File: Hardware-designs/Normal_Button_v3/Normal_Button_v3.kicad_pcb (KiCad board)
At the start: 2 copper layers, 74.2 x 74.2 mm, 40 parts, among them J1 UART, J2 Bat, J3 USB_C, Q1 MMBT3904, SW1 main, SW2 Aux, SW3 Side 1, SW4 Side 2, U1 ESP32-WROOM-32, U2 TP4057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

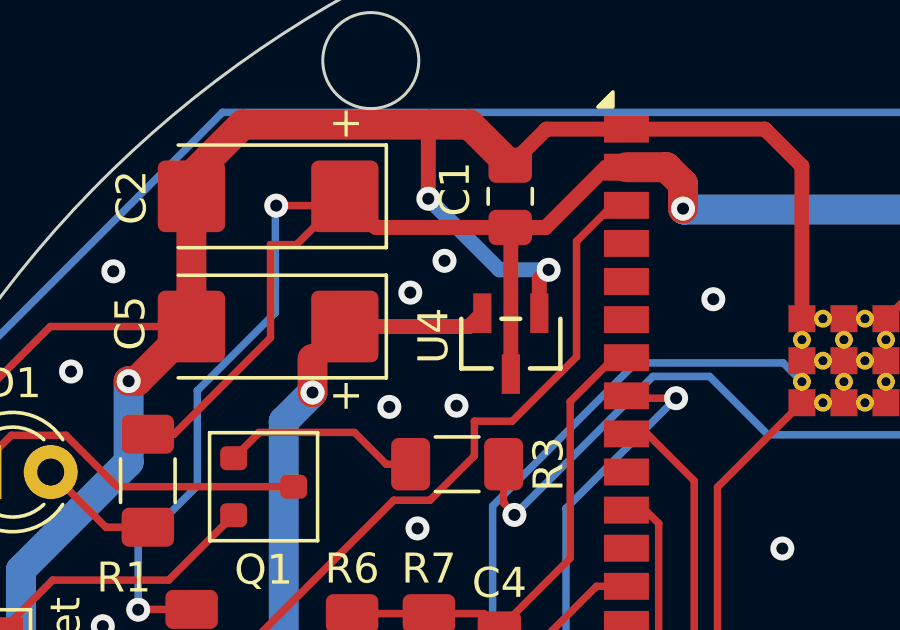
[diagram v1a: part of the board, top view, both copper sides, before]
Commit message: correction voltage regulator
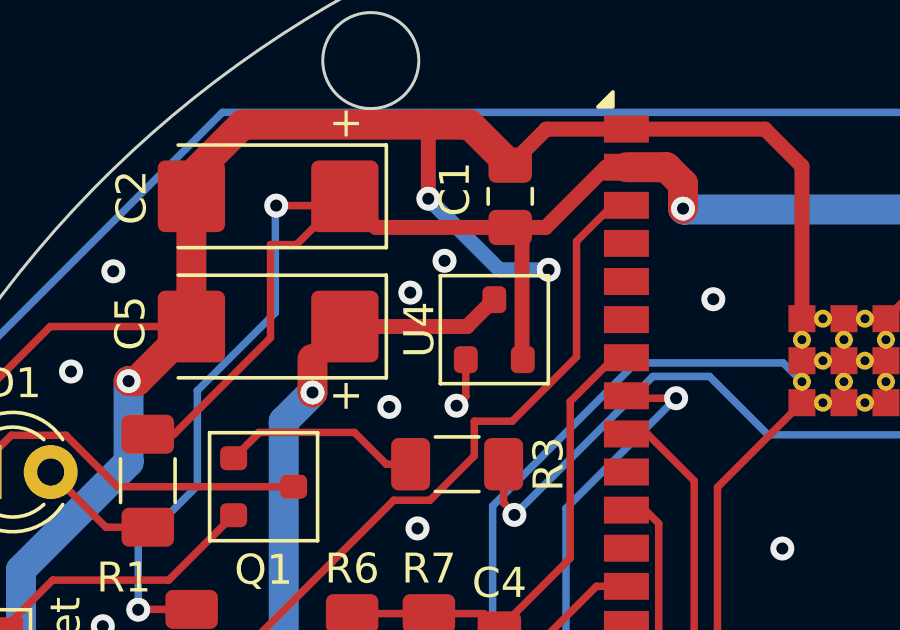
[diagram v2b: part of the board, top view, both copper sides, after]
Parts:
- U4: value MCP1700 -> MCP1700T-3302E/TT; footprint MCP1700T_3302E_TT 3:SOT-23_MC_MCH -> PCM_Package_TO_SOT_SMD_AKL:SOT-23
- moved U4 0.72 mm to (139.5, 59.5), turned to 90 degrees
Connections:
- U4 pad 2: +BATT -> +3.3V
- U4 pad 3: +3.3V -> +BATT
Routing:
- net +BATT: track 104.5 -> 105.1 mm

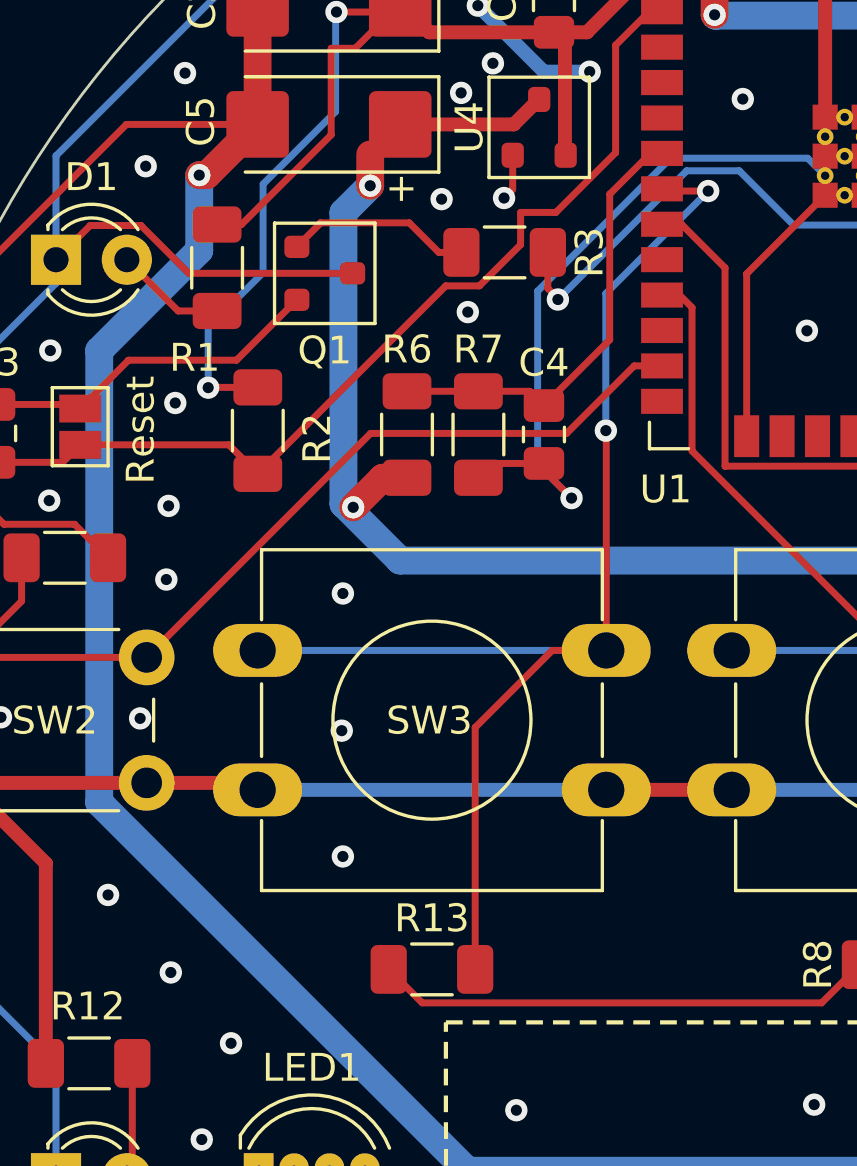
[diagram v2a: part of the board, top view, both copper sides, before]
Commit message: correction voltage regulator
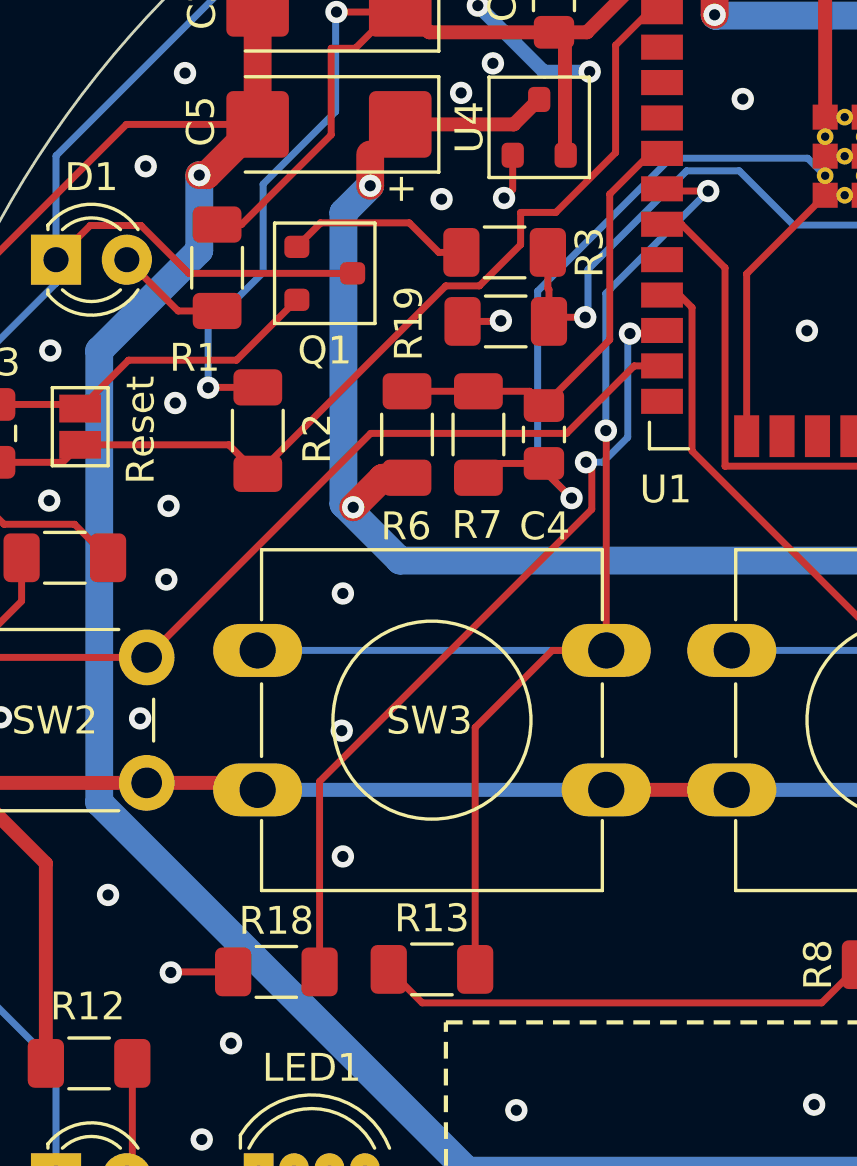
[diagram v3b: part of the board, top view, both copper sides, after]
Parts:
- added R18: 10k, Resistor_SMD:R_1206_3216Metric_Pad1.30x1.75mm_HandSolder, F.Cu at (130.1, 89.8)
- added R19: 100k, Resistor_SMD:R_1206_3216Metric_Pad1.30x1.75mm_HandSolder, F.Cu at (138.3, 66.5)
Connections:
- U1 pad 12: unconnected-(U1-IO27-Pad12) -> Net-(U1-IO27)
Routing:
- net Net-(U1-IO27): track 0.00 -> 29.3 mm, vias 0 -> 2
- net GND: track 335.0 -> 338.7 mm
- net Net-(U1-IO18): track 26.0 -> 28.1 mm

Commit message: Magnetic Sensor
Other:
- board text added: "HueMix Link V3.0 Rev. B"
- board text added: "March 2026"
- board text removed: "February 2026"
- board text removed: "HueMix Link V3.0"
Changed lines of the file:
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@@
 		)
 	)
-	(gr_text "HueMix Link\nV3.0\n"
+	(gr_text "HueMix Link\nV3.0 Rev. B\n"
 		(at 152.654 55.118 0)
 		(layer "B.SilkS")
@@
 		)
 	)
-	(gr_text "February 2026\n"
+	(gr_text "March 2026\n"
 		(at 152.654 107.95 0)
 		(layer "B.SilkS")
@@
 			(font
 				(size 2 2)
-				(thickness 0.3)
+				(thickness 0.25)
 			)
 			(justify mirror)

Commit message: Minor KiCad files update for all devices
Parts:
- C3: value 1nF -> 68nF
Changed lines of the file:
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@@
 			)
 		)
-		(property "Value" "1nF"
+		(property "Value" "68nF"
 			(at 0 1.68 90)
 			(layer "F.Fab")
